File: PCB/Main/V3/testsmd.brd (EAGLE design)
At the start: 37.5 x 34.4 mm, 14 parts, among them J1 FEMALE 2x3

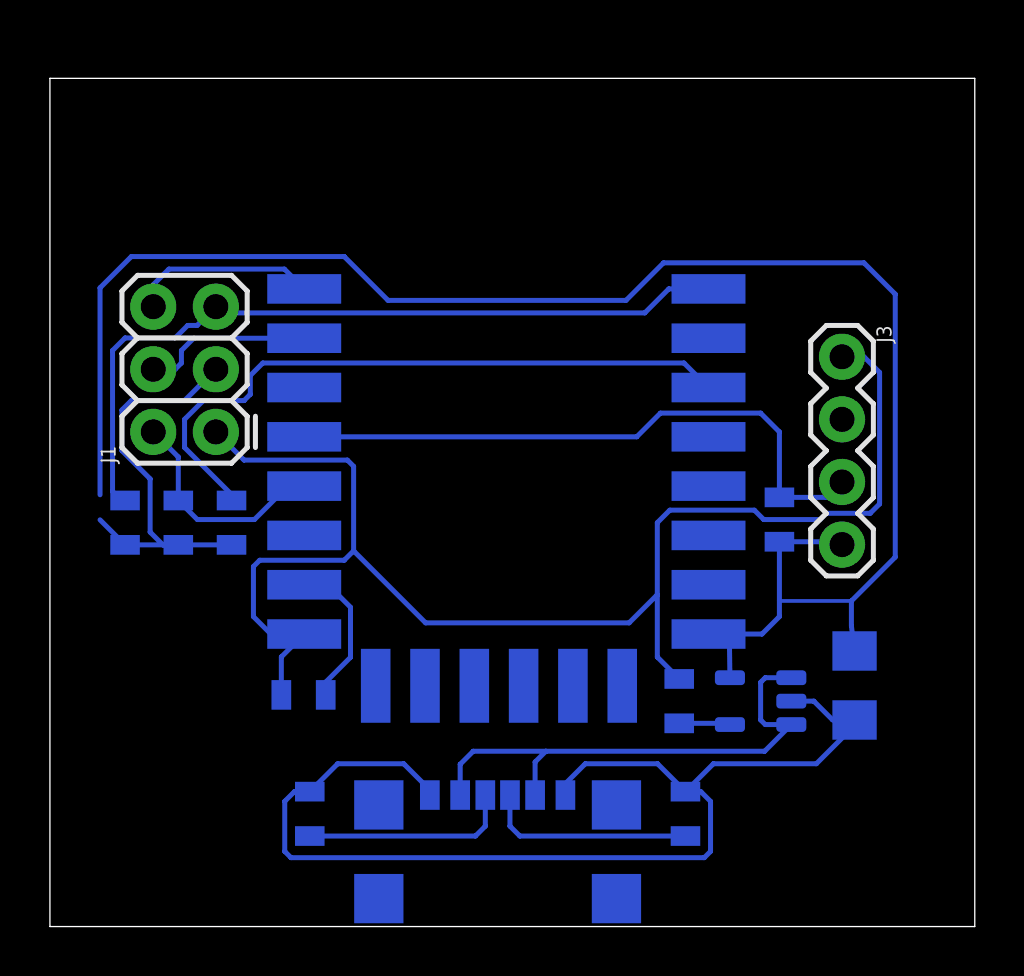
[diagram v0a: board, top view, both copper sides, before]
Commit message: Changing the board layout and adding capability to read V_BUS
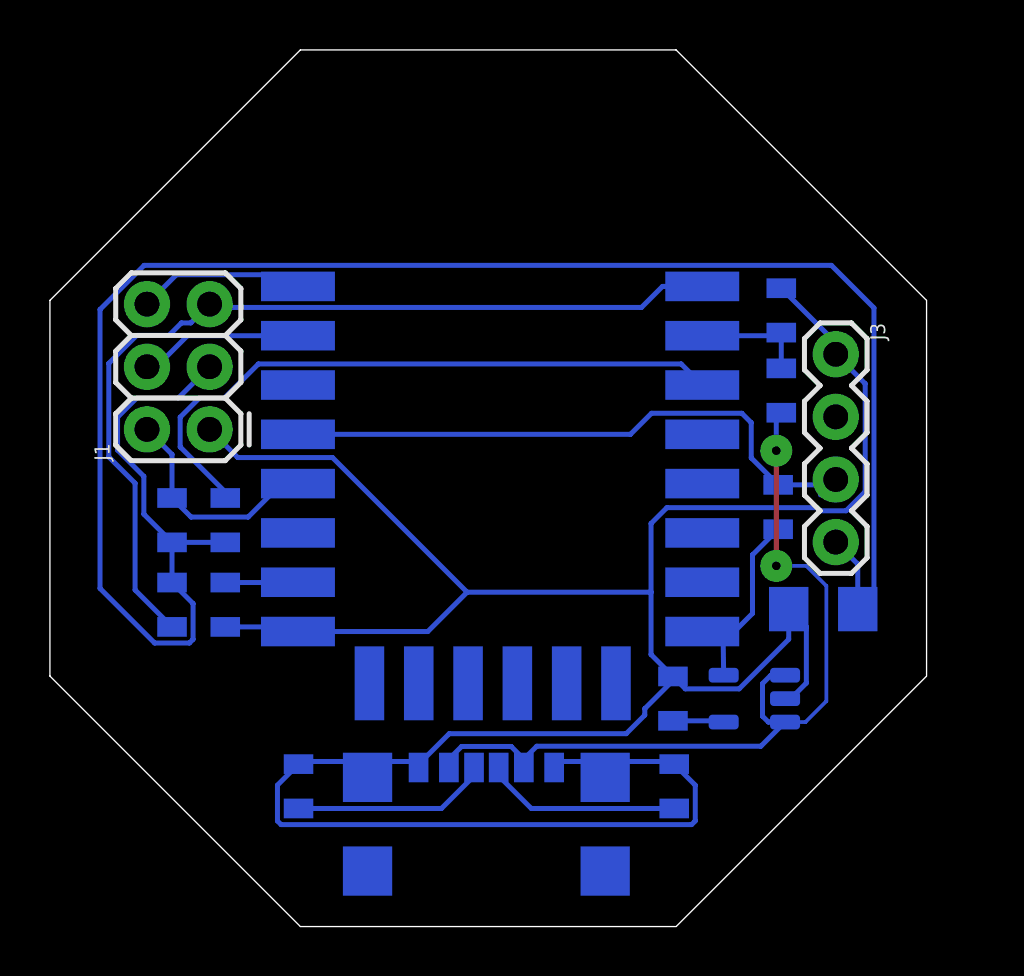
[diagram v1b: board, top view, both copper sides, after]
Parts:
- added R6: 5.1k, SparkFun-Resistors:0805
- added R7: 1k, SparkFun-Resistors:0805
- moved R4 4.84 mm to (7.11, 13.1), turned to 90 degrees
- moved R1 3.83 mm to (4.95, 13.1), turned to 90 degrees
- moved C2 3.35 mm to (31.4, 12.9), turned to 0 degrees
- moved R8 1.21 mm to (25.3, 5.69)
- moved R9 1.21 mm to (10.1, 5.69)
- moved U$3 1.21 mm to (17.7, 6.45)
- moved R5 0.51 mm to (29.5, 17.0)
- moved C1 0.27 mm to (25.3, 9.25)
- moved U$1 0.27 mm to (28.6, 9.25)
- moved J3 0.27 mm to (31.9, 23.2)
- moved J1 0.27 mm to (6.48, 20.2)
- moved R2 0.27 mm to (7.11, 16.5)
- moved R3 0.27 mm to (4.95, 16.5)
- moved U1 0.27 mm to (18.2, 20.2)
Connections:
- new net N$9: R6.1, R7.2, U1.ADC
- net 5V: now also R6.2
- net GND: now also R7.1
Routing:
- net 5V: track 21.5 -> 34.1 mm, vias 0 -> 2
- net GND: track 106.2 -> 114.4 mm
- net N$3: track 31.8 -> 37.2 mm
- net N$9: track 0.00 -> 4.71 mm
- net N$1: track 6.23 -> 3.92 mm
- net 3.3V: track 88.9 -> 90.7 mm
- net N$2: track 7.61 -> 6.81 mm
- net N$4: track 27.1 -> 26.5 mm
- net N$12: track 8.55 -> 8.01 mm
- net N$11: track 8.55 -> 8.01 mm
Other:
- board size 37.5 x 34.4 mm -> 35.6 x 35.6 mm
